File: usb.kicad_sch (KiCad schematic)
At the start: 21 parts, among them J2 TYPE-C 16PIN 2MD(073), U3 TPS25200DRVT, U4 USBLC6-2P6, U5 USBLC6-2P6

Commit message: final shipped rev1 bentoboard
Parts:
- U4, U5: LCSC Part C15999 -> C2827693
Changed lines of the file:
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@@
 			)
 		)
-		(property "LCSC Part" "C15999"
+		(property "LCSC Part" "C2827693"
 			(at 195.58 86.36 0)
 			(effects
@@
 			)
 		)
-		(property "LCSC Part" "C15999"
+		(property "LCSC Part" "C2827693"
 			(at 195.58 114.3 0)
 			(effects

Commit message: oops fix: reversed diodes
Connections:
- net GND: now also D4.2 (A); no longer D4.1 (K)
- net VBUS_RAW: now also D4.1 (K); no longer D4.2 (A)
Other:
- moved on the sheet: D4
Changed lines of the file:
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@@
 	(symbol
 		(lib_id "Device:D_Zener_Small")
-		(at 77.47 143.51 90)
+		(at 77.47 143.51 270)
 		(unit 1)
 		(exclude_from_sim no)
@@
 					(size 1.27 1.27)
 				)
-				(justify right)
+				(justify left)
 			)
 		)
@@
 					(size 1.27 1.27)
 				)
-				(justify right)
+				(justify left)
 			)
 		)

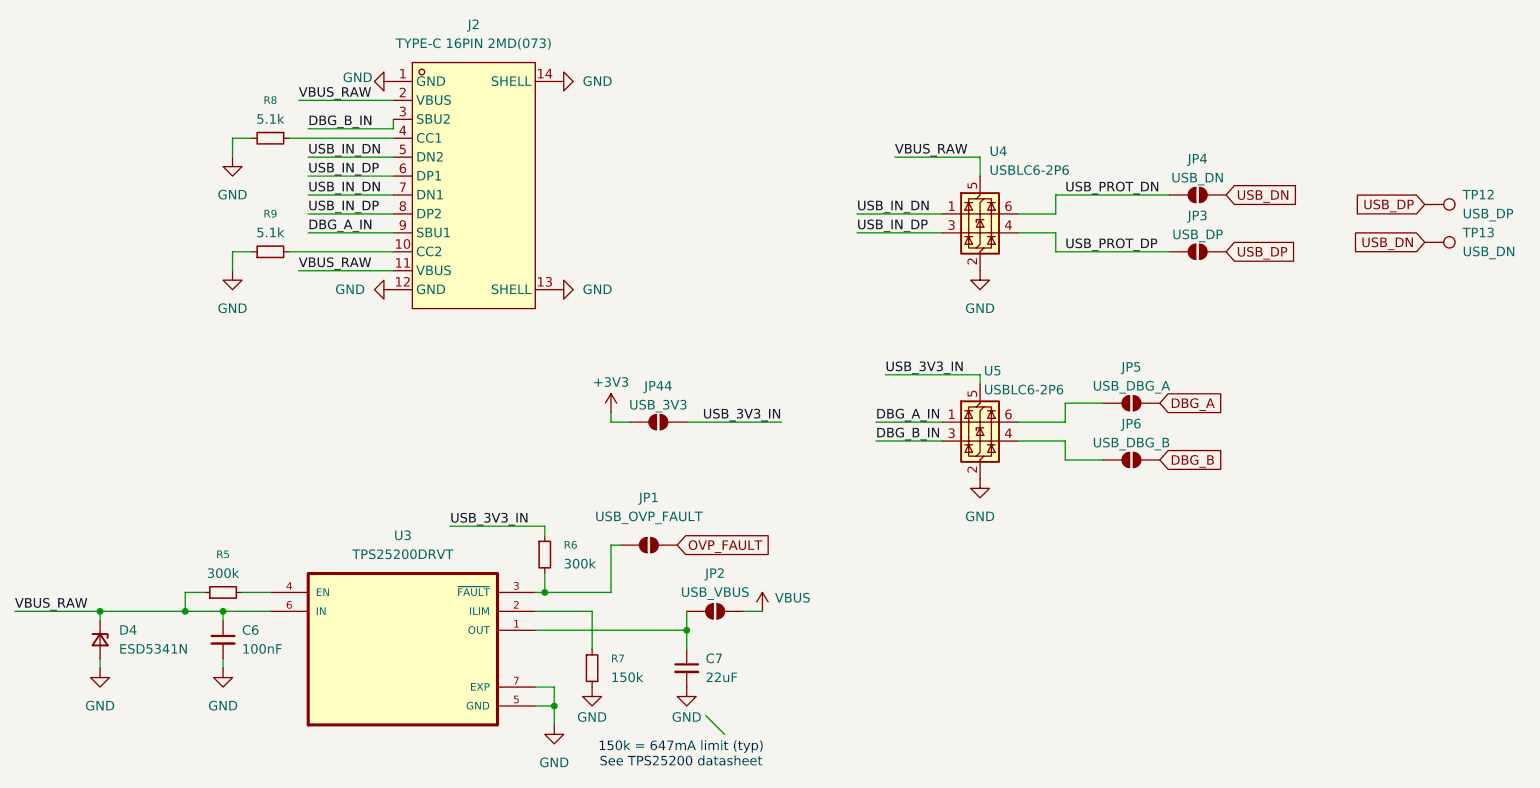
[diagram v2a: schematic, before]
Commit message: remove all jumpers
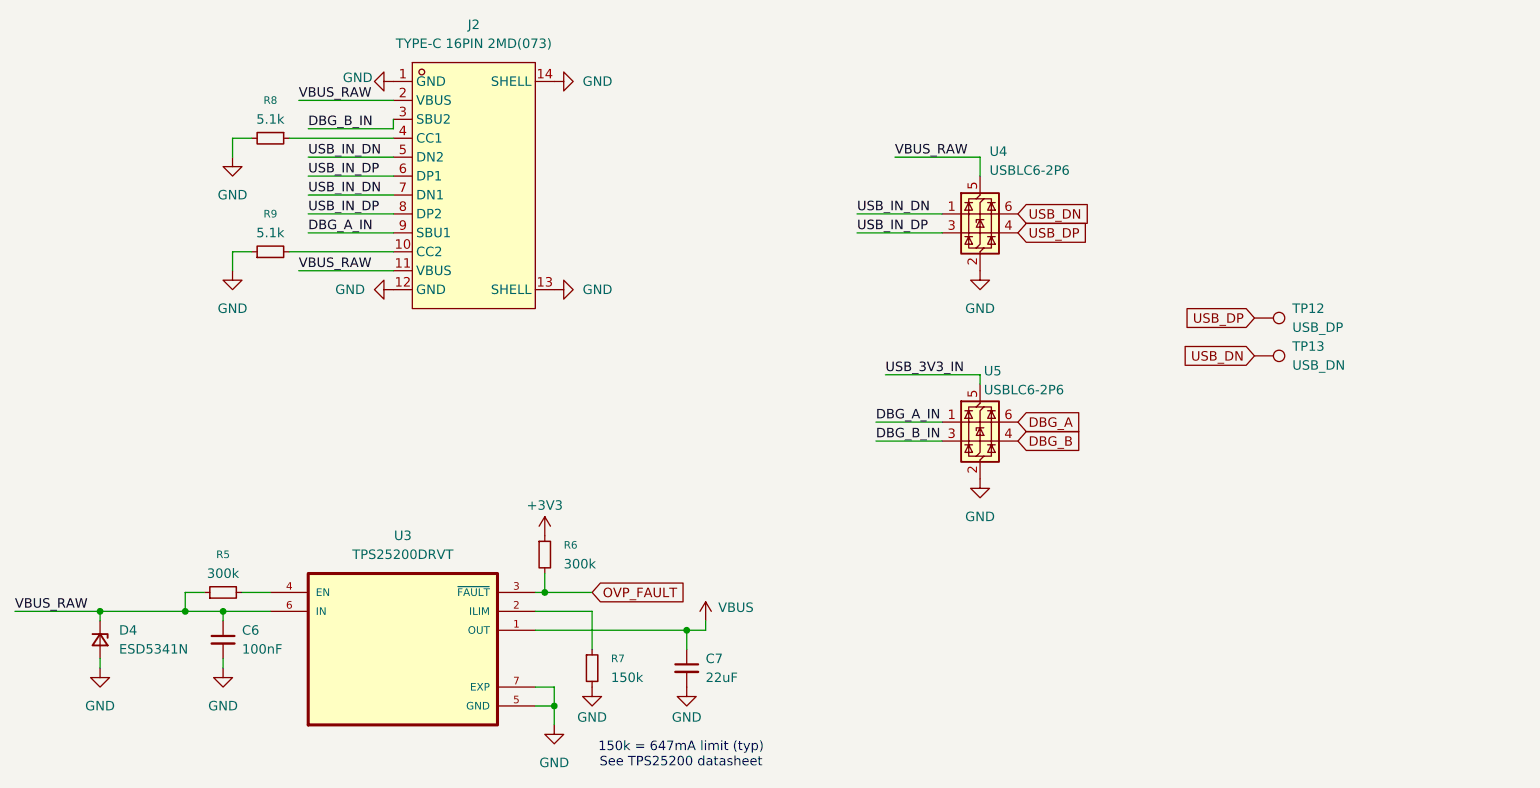
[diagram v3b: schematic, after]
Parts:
- removed JP1: USB_OVP_FAULT, Jumper:SolderJumper-2_P1.3mm_Open_Pad1.0x1.5mm, symbol Jumper:SolderJumper_2_Open
- removed JP2: USB_VBUS, Jumper:SolderJumper-2_P1.3mm_Open_Pad1.0x1.5mm, symbol Jumper:SolderJumper_2_Open
- removed JP3: USB_DP, Jumper:SolderJumper-2_P1.3mm_Open_Pad1.0x1.5mm, symbol Jumper:SolderJumper_2_Open
- removed JP4: USB_DN, Jumper:SolderJumper-2_P1.3mm_Open_Pad1.0x1.5mm, symbol Jumper:SolderJumper_2_Open
- removed JP44: USB_3V3, Jumper:SolderJumper-2_P1.3mm_Open_Pad1.0x1.5mm, symbol Jumper:SolderJumper_2_Open
- removed JP5: USB_DBG_A, Jumper:SolderJumper-2_P1.3mm_Open_Pad1.0x1.5mm, symbol Jumper:SolderJumper_2_Open
- removed JP6: USB_DBG_B, Jumper:SolderJumper-2_P1.3mm_Open_Pad1.0x1.5mm, symbol Jumper:SolderJumper_2_Open
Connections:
- net USB_PROT_DN is gone; now on net USB_DN: U4.6 (I/O1)
- net USB_PROT_DP is gone; now on net USB_DP: U4.4 (I/O2)
- net +3V3: now also R6.1
- net DBG_A: now also U5.6 (I/O1)
- net DBG_B: now also U5.4 (I/O2)
- net OVP_FAULT: now also R6.2, U3.3 (~{FAULT})
- net USB_3V3_IN: no longer R6.1
- net VBUS: now also C7.1, U3.1 (OUT)
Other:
- moved on the sheet: TP12, TP13

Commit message: progress 2
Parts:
- C7: footprint Capacitor_SMD:C_0603_1608Metric -> Capacitor_SMD:C_0402_1005Metric; LCSC Part C59461 -> (none)
- R5, R6: footprint Resistor_SMD:R_0603_1608Metric -> Resistor_SMD:R_0402_1005Metric; LCSC Part C23024 -> (none)
- R7: footprint Resistor_SMD:R_0603_1608Metric -> Resistor_SMD:R_0402_1005Metric; LCSC Part C22807 -> (none)
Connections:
- net USB_3V3_IN is gone; now on net +3V3: U5.5 (VBUS)
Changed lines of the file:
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@@
-	(wire
-		(pts
-			(xy 195.58 107.95) (xy 195.58 109.22)
-		)
-		(stroke
-			(width 0)
-			(type default)
-		)
-	)
 	(wire
 		(pts
@@
 		(pts
 			(xy 102.87 76.2) (xy 116.84 76.2)
-		)
-		(stroke
-			(width 0)
-			(type default)
-		)
-	)
-	(wire
-		(pts
-			(xy 182.88 107.95) (xy 195.58 107.95)
 		)
 		(stroke
@@
 	(label "USB_IN_DP"
 		(at 105.41 86.36 0)
-		(effects
-			(font
-				(size 1.27 1.27)
-			)
-			(justify left bottom)
-		)
-	)
-	(label "USB_3V3_IN"
-		(at 182.88 107.95 0)
 		(effects
 			(font
@@
 			)
 		)
-		(property "Footprint" "Capacitor_SMD:C_0603_1608Metric"
+		(property "Footprint" "Capacitor_SMD:C_0402_1005Metric"
 			(at 156.21 147.32 0)
 			(effects
@@
 			)
 		)
-		(property "LCSC Part" "C59461"
+		(property "LCSC Part" ""
 			(at 156.21 147.32 0)
 			(effects
@@
 			)
 		)
-		(property "Footprint" "Resistor_SMD:R_0603_1608Metric"
+		(property "Footprint" "Resistor_SMD:R_0402_1005Metric"
 			(at 143.51 147.32 0)
 			(effects
@@
 			)
 		)
-		(property "LCSC Part" "C22807"
+		(property "LCSC Part" ""
 			(at 143.51 147.32 0)
 			(effects
@@
 			)
 		)
-		(property "Footprint" "Resistor_SMD:R_0603_1608Metric"
+		(property "Footprint" "Resistor_SMD:R_0402_1005Metric"
 			(at 93.98 137.16 0)
 			(effects
@@
 			)
 		)
-		(property "LCSC Part" "C23024"
+		(property "LCSC Part" ""
 			(at 93.98 137.16 90)
 			(effects
@@
 		(dnp no)
 		(property "Reference" "U5"
-			(at 196.088 107.442 0)
+			(at 198.12 107.442 0)
 			(effects
 				(font
@@
 		)
 		(property "Value" "USBLC6-2P6"
-			(at 196.088 109.982 0)
+			(at 198.12 109.982 0)
 			(effects
 				(font
@@
 	)
 	(symbol
+		(lib_id "power:+3V3")
+		(at 195.58 109.22 0)
+		(unit 1)
+		(exclude_from_sim no)
+		(in_bom yes)
+		(on_board yes)
+		(dnp no)
+		(property "Reference" "#PWR06"
+			(at 195.58 113.03 0)
+			(effects
+				(font
+					(size 1.27 1.27)
+				)
+				(hide yes)
+			)
+		)
+		(property "Value" "+3V3"
+			(at 195.58 105.664 0)
+			(effects
+				(font
+					(size 1.27 1.27)
+				)
+			)
+		)
+		(property "Footprint" ""
+			(at 195.58 109.22 0)
+			(effects
+				(font
+					(size 1.27 1.27)
+				)
+				(hide yes)
+			)
+		)
+		(property "Datasheet" ""
+			(at 195.58 109.22 0)
+			(effects
+				(font
+					(size 1.27 1.27)
+				)
+				(hide yes)
+			)
+		)
+		(property "Description" "Power symbol creates a global label with name \"+3V3\""
+			(at 195.58 109.22 0)
+			(effects
+				(font
+					(size 1.27 1.27)
+				)
+				(hide yes)
+			)
+		)
+		(pin "1"
+		)
+		(instances
+			(project ""
+				(path "/c6cb5a1d-9f97-4766-8582-a9e93ed049e4/69f5d0af-289d-4671-84fe-e5e630f97c44"
+					(reference "#PWR06")
+					(unit 1)
+				)
+			)
+		)
+	)
+	(symbol
 		(lib_id "Connector:TestPoint")
 		(at 232.41 100.33 270)
@@
 			)
 		)
-		(property "Footprint" "Resistor_SMD:R_0603_1608Metric"
+		(property "Footprint" "Resistor_SMD:R_0402_1005Metric"
 			(at 137.16 132.08 0)
 			(effects
@@
 			)
 		)
-		(property "LCSC Part" "C23024"
+		(property "LCSC Part" ""
 			(at 137.16 132.08 0)
 			(effects

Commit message: final fixups before prod
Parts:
- removed TP12: USB_DP, TestPoint:TestPoint_Pad_D1.0mm, symbol Connector:TestPoint
- removed TP13: USB_DN, TestPoint:TestPoint_Pad_D1.0mm, symbol Connector:TestPoint
- C19: renamed from C7; LCSC Part (none) -> C47339
- R3: renamed from R5; LCSC Part (none) -> C25774
- R6: LCSC Part (none) -> C25774
- R7: LCSC Part (none) -> C2909320
- renumbered C6 to C18, D4 to D1, J2 to J1, R8 to R4, R9 to R5
